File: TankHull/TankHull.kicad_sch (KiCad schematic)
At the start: 62 parts, among them J1 SlipRing_6, J10 Conn_01x02_Socket, J2 Conn_01x02_Socket, J3 Conn_01x02_Socket, J4 Conn_01x02_Socket, J5 Conn_01x02_Socket, J7 Conn_01x05, J8 Conn_01x02_Socket, J9 Conn_01x02_Socket, Q1 Q_PMOS, U1 PCA9685PW, U2 DRV8833PWP, U3 DRV8833PWP

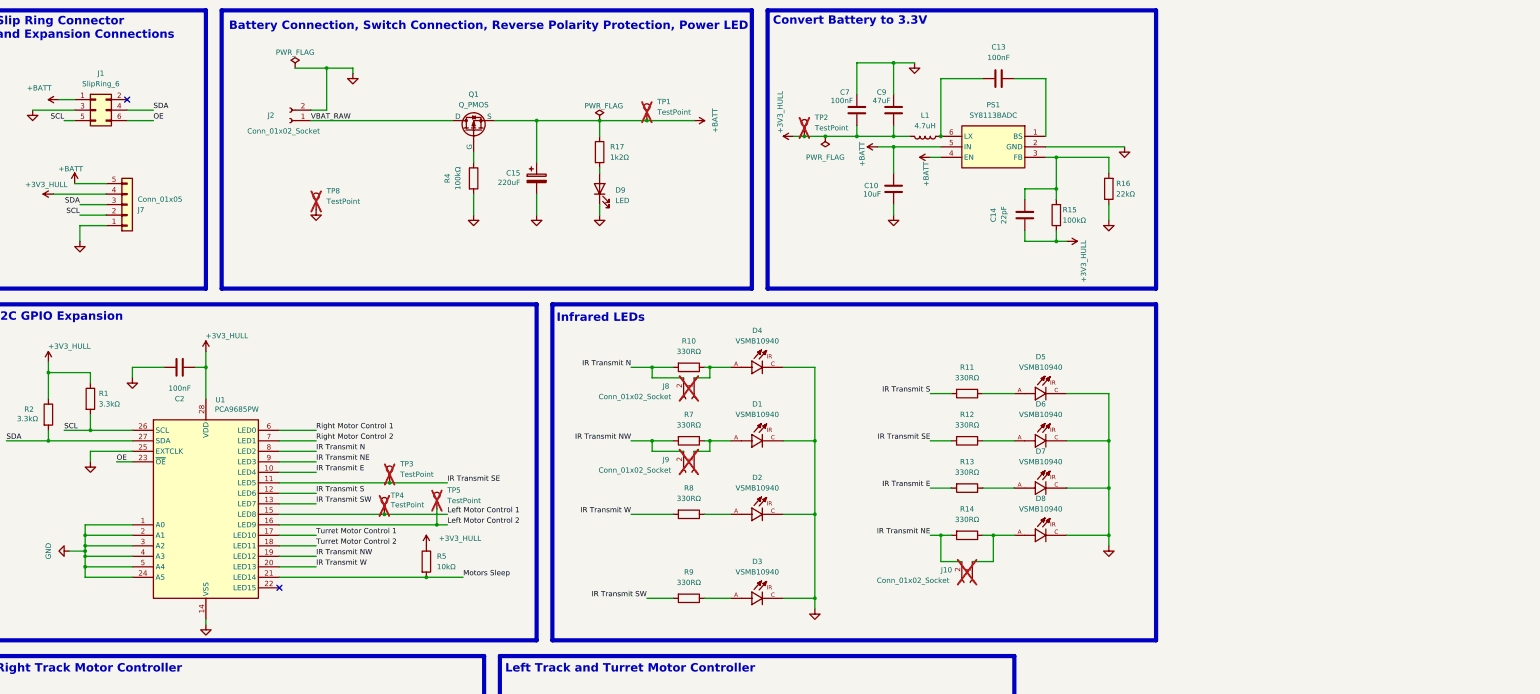
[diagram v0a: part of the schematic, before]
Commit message: began IR receiver update on hull board
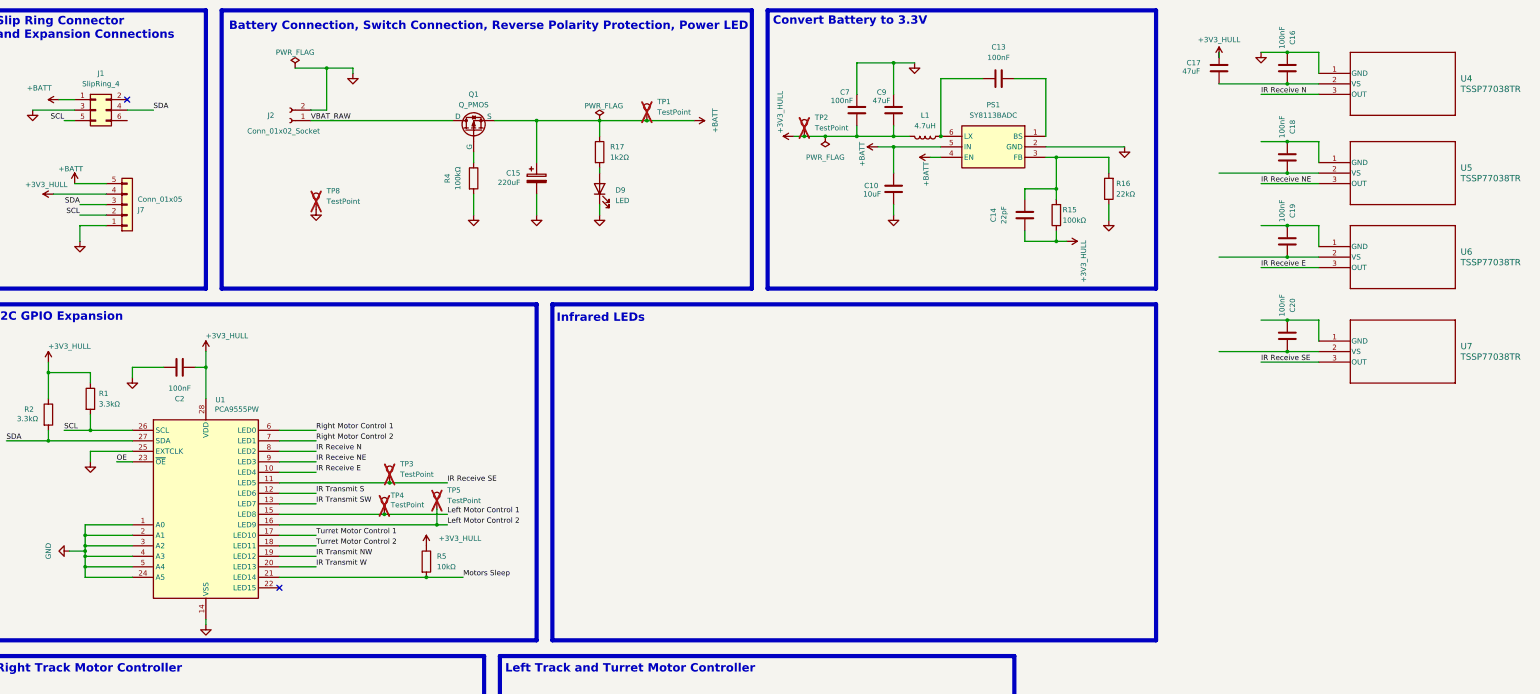
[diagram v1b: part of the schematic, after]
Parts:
- removed D1, D2, D3, D4, D5, D6, D7, D8: VSMB10940, Thundergeddon:DIO_VSMB10940, symbol VishayLED:VSMB10940
- removed J10, J8, J9: Conn_01x02_Socket, Connector_PinHeader_2.54mm:PinHeader_1x02_P2.54mm_Vertical, symbol Connector:Conn_01x02_Socket
- removed R10, R11, R12, R13, R14, R7, R8, R9: 330RΩ, Resistor_SMD:R_0603_1608Metric, symbol Device:R
- added C16, C18, C19, C20: 100nF, Capacitor_SMD:C_0603_1608Metric, symbol Device:C
- added C17: 47uF, Capacitor_SMD:C_0805_2012Metric, symbol Device:C
- added U4, U5, U6, U7: TSSP77038TR, Vishay IR receiver:TSSP77038TR_VIS, symbol Vishay IR Receiver:TSSP77038TR
- J1: value SlipRing_6 -> SlipRing_4; footprint Connector_JST:JST_XH_B6B-XH-A_1x06_P2.50mm_Vertical -> Connector_JST:JST_XH_B4B-XH-A_1x04_P2.50mm_Vertical; JLCPCB Part # C2908604 -> C2908602; Manufacturer_Part_Number XH-6A -> XH-4A
- U1: value PCA9685PW -> PCA9555PW; footprint Package_SO:TSSOP-28_4.4x9.7mm_P0.65mm -> Package_SO:TSSOP-24-1EP_4.4x7.8mm_P0.65mm_EP3.2x5mm; JLCPCB Part # C2678753 -> C128392; Manufacturer_Part_Number PCA9685PW,118 -> PCA9555PW,118
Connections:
- net +3V3_HULL: now also C17.2
- net GND: now also C16.1, U4.1 (GND)
- net OE: no longer J1.6 (Pin_6)
- net IR Transmit E renamed IR Receive E
- net IR Receive E: now also U6.3 (OUT)
- net IR Transmit N renamed IR Receive N
- net IR Receive N: now also U4.3 (OUT)
- net IR Transmit NE renamed IR Receive NE
- net IR Receive NE: now also U5.3 (OUT)
- net IR Transmit SE renamed IR Receive SE
- net IR Receive SE: now also U7.3 (OUT)
- new net: C19.1, U6.1 (GND)
- new net: C19.2, U6.2 (VS)
- new net: C16.2, C17.1, U4.2 (VS)
- new net: C18.1, U5.1 (GND)
- new net: C18.2, U5.2 (VS)
- new net: C20.1, U7.1 (GND)
- new net: C20.2, U7.2 (VS)

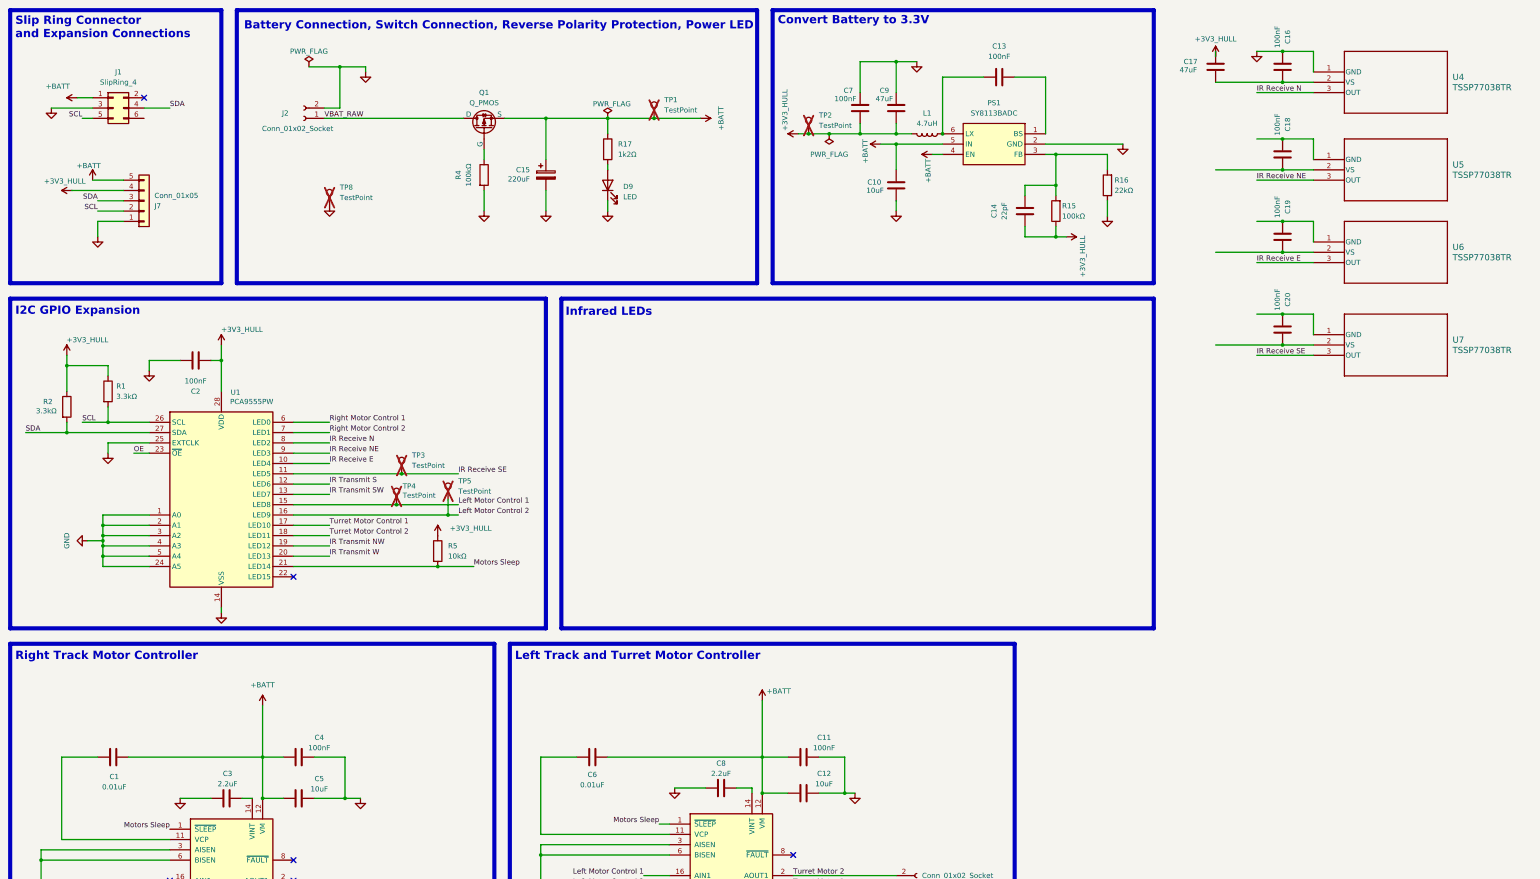
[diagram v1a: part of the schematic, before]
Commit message: continue with ir receiver update
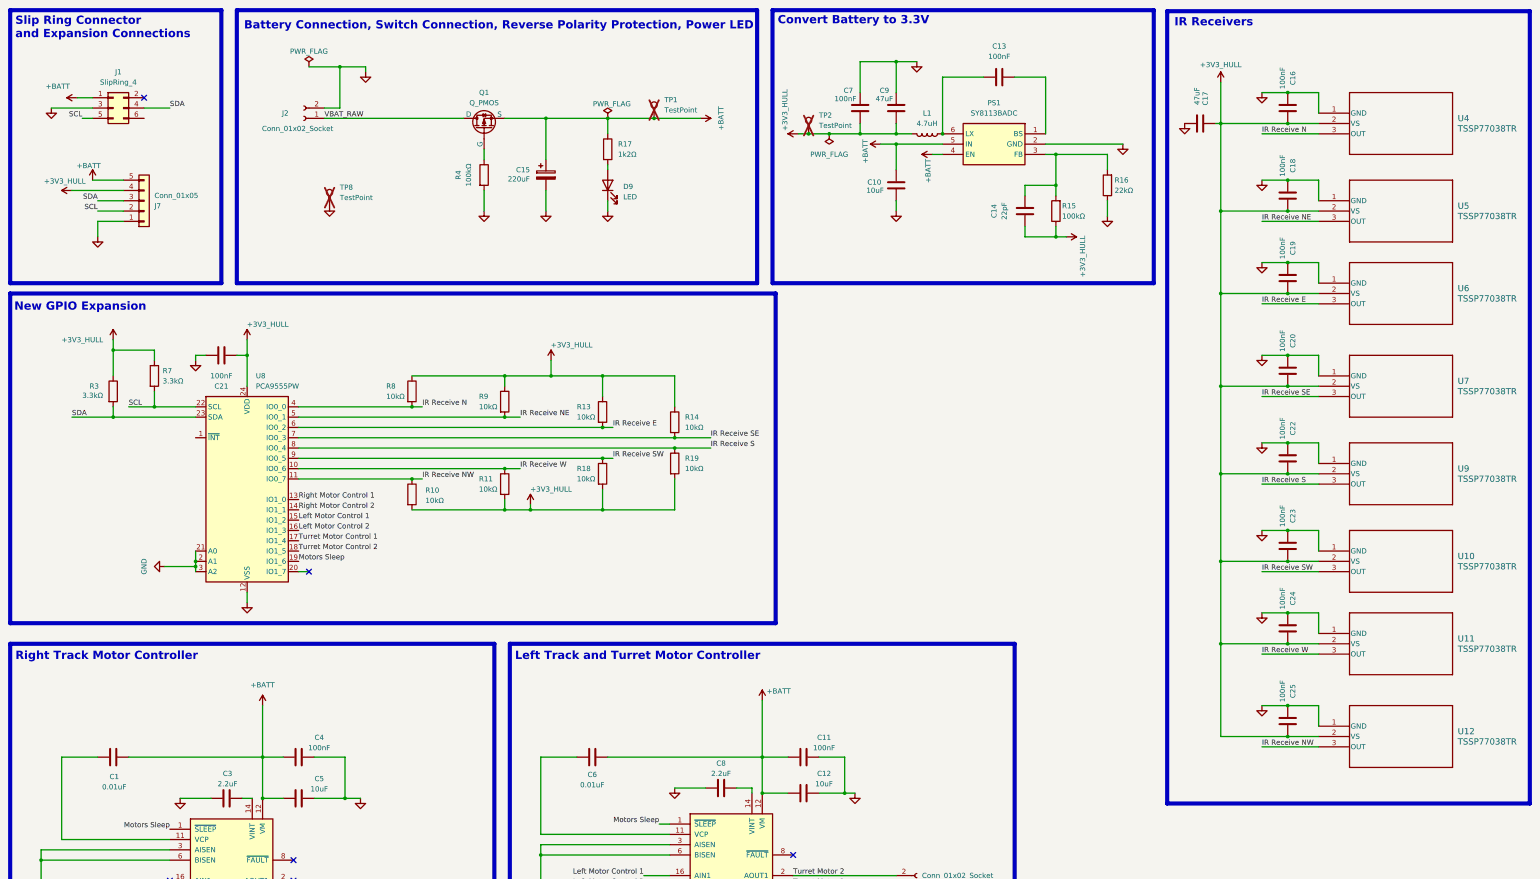
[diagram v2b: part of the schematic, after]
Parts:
- removed C2: 100nF, Capacitor_SMD:C_0603_1608Metric, symbol Device:C
- removed R1, R2: 3.3kΩ, Resistor_SMD:R_0603_1608Metric, symbol Device:R
- removed R5: 10kΩ, Resistor_SMD:R_0603_1608Metric, symbol Device:R
- removed TP3, TP4, TP5: TestPoint, TestPoint:TestPoint_Pad_D1.0mm, symbol Connector:TestPoint
- removed U1: PCA9555PW, Package_SO:TSSOP-24-1EP_4.4x7.8mm_P0.65mm_EP3.2x5mm, symbol Driver_LED:PCA9685PW
- added C21, C22, C23, C24, C25: 100nF, Capacitor_SMD:C_0603_1608Metric, symbol Device:C
- added R10, R11, R13, R14, R18, R19, R8, R9: 10kΩ, Resistor_SMD:R_0603_1608Metric, symbol Device:R
- added R3, R7: 3.3kΩ, Resistor_SMD:R_0603_1608Metric, symbol Device:R
- added U10, U11, U12, U9: TSSP77038TR, Vishay IR receiver:TSSP77038TR_VIS, symbol Vishay IR Receiver:TSSP77038TR
- added U8: PCA9555PW, Package_SO:TSSOP-24_4.4x7.8mm_P0.65mm, symbol Interface_Expansion:PCA9555PW
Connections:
- net +3V3_HULL: now also C16.2, C18.2, C19.2, C20.2, U4.2 (VS), U5.2 (VS), U6.2 (VS), U7.2 (VS), C21.2, C22.2, C23.2, C24.2, C25.2, R10.2, R11.2, R13.1, R14.1, R18.2, R19.2, R3.1, R7.1, R8.1, R9.1, U10.2 (VS), U11.2 (VS), U12.2 (VS), U8.24 (VDD), U9.2 (VS)
- net GND: now also C17.1, C18.1, C19.1, C20.1, U5.1 (GND), U6.1 (GND), U7.1 (GND), C21.1, C22.1, C23.1, C24.1, C25.1, U10.1 (GND), U11.1 (GND), U12.1 (GND), U8.12 (VSS), U8.2 (A1), U8.21 (A0), U8.3 (A2), U9.1 (GND)
- net IR Receive E: now also R13.2, U8.6 (IO0_2)
- net IR Receive N: now also R8.2, U8.4 (IO0_0)
- net IR Receive NE: now also R9.2, U8.5 (IO0_1)
- net IR Receive SE: now also R14.2, U8.7 (IO0_3)
- net Left Motor Control 1: now also U8.15 (IO1_2)
- net Left Motor Control 2: now also U8.16 (IO1_3)
- net Motors Sleep: now also U8.19 (IO1_6)
- net Right Motor Control 1: now also U8.13 (IO1_0)
- net Right Motor Control 2: now also U8.14 (IO1_1)
- net SCL: now also R7.2, U8.22 (SCL)
- net SDA: now also R3.2, U8.23 (SDA)
- net Turret Motor Control 1: now also U8.17 (IO1_4)
- net Turret Motor Control 2: now also U8.18 (IO1_5)
- new net IR Receive NW: R10.1, U12.3 (OUT), U8.11 (IO0_7)
- new net IR Receive S: R19.1, U8.8 (IO0_4), U9.3 (OUT)
- new net IR Receive SW: R18.1, U10.3 (OUT), U8.9 (IO0_5)
- new net IR Receive W: R11.1, U11.3 (OUT), U8.10 (IO0_6)
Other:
- note added: "IR Receivers"
- note added: "New GPIO Expansion"
- note removed: "I2C GPIO Expansion"
- note removed: "Infrared LEDs"
- moved on the sheet: C16, C17, C18, C19, C20, U4, U5, U6, U7
